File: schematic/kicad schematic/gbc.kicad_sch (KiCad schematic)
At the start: 19 parts, among them P1 Cart Connector, U1 CGB CPU, U6 PST9135N, X1 Crystal_Small

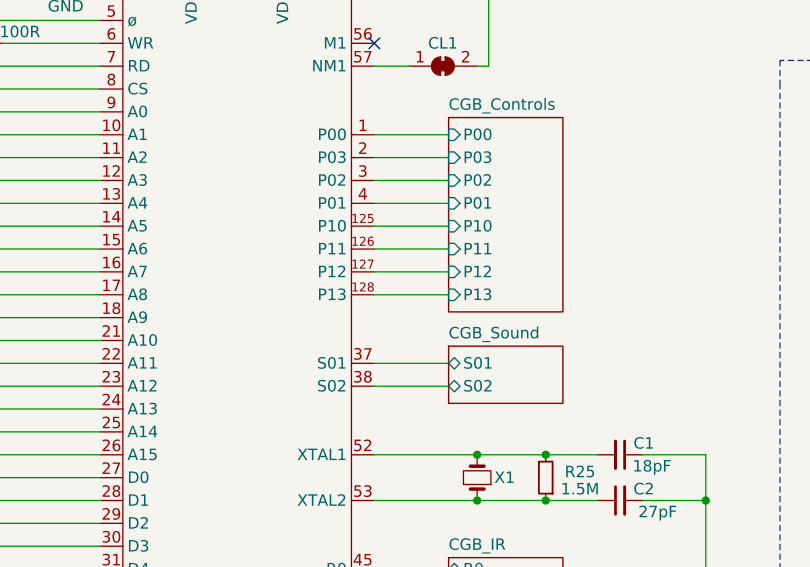
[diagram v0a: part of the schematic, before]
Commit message: fixed schematic, thx giltesa and darren
the ir transistor was labelled wrong
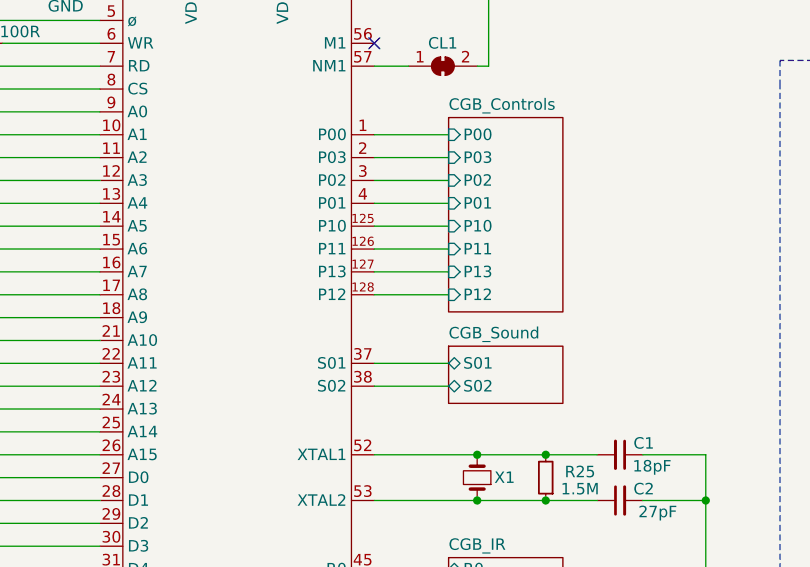
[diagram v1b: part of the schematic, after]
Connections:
- net CGB_Controls/P12: now also U1.128 (P12); no longer U1.127 (P12)
- net CGB_Controls/P13: now also U1.127 (P13); no longer U1.128 (P13)
